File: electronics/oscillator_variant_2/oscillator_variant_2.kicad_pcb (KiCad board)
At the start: 2 copper layers, 42.5 x 46.2 mm, 51 parts, among them J1 module_2x15_left_input, J2 module_2x15_right_input, J3 Coax, Q1 BC817, U1 TL081, U2 LME49720, U3 TL082, U4 TL431

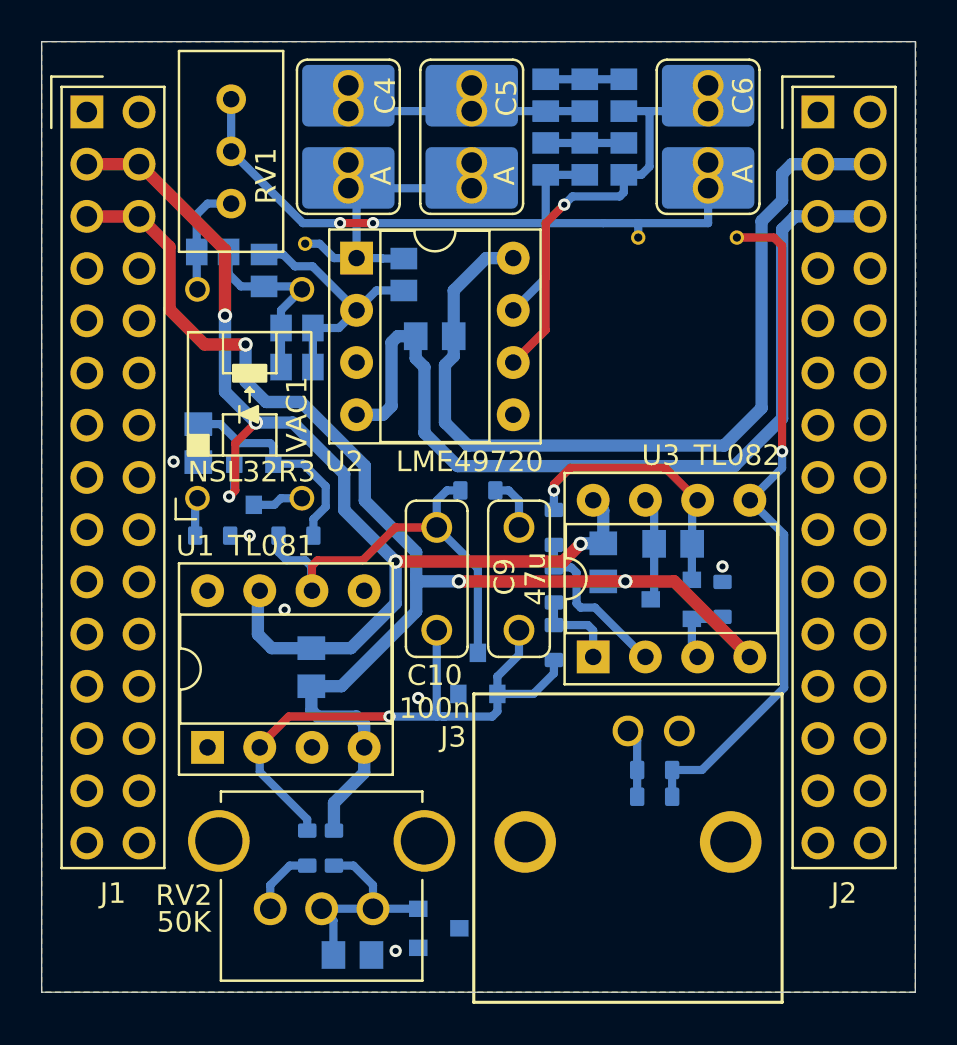
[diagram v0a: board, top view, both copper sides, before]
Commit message: added oscillator variant with dual single opamp
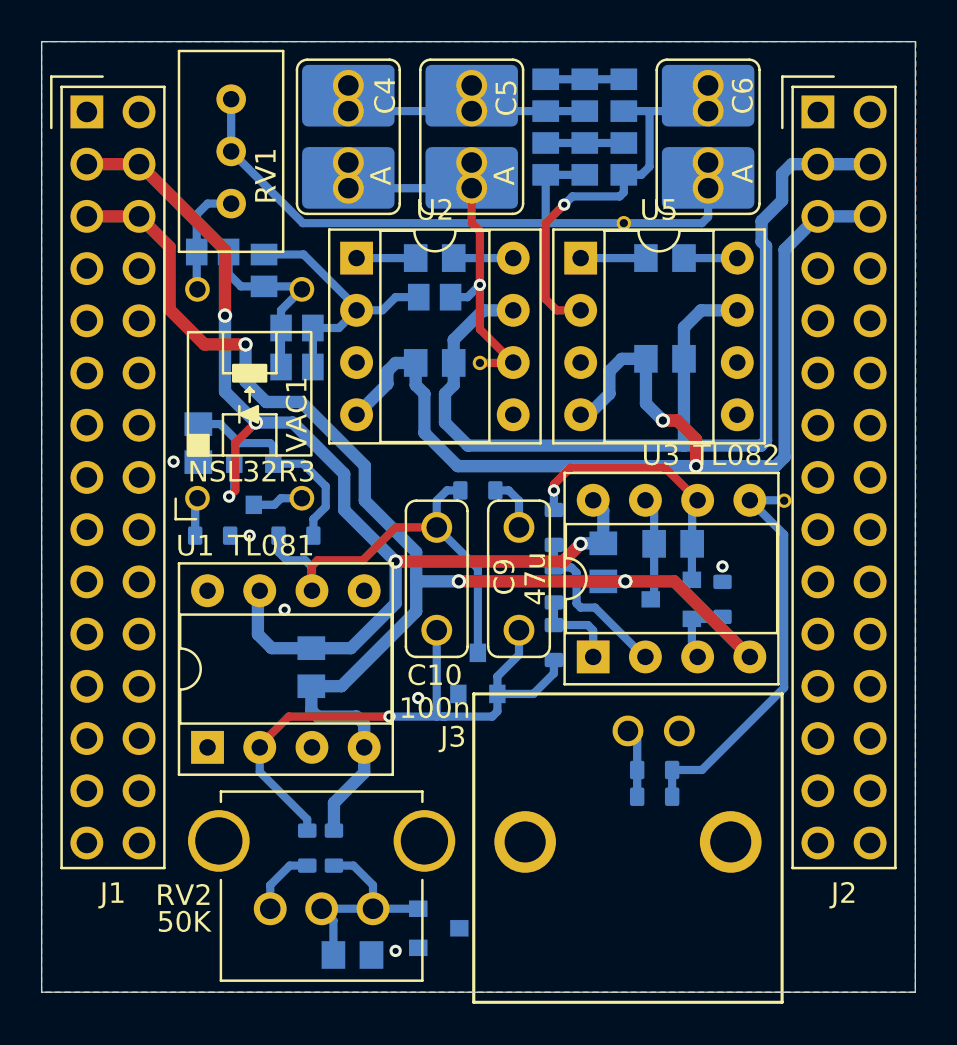
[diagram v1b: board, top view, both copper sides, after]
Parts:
- added C12: 22p, SquantorRcl:C_0805+0603, B.Cu at (161.7, 79.5)
- added C13: 10u, SquantorRcl:C_0805+0603, B.Cu at (172.9, 84.4)
- added C14: 22p, SquantorRcl:C_0805+0603, B.Cu at (172.9, 79.5)
- added U5: NE5534, Package_DIP:DIP-8_W7.62mm_Socket, F.Cu at (168.8, 79.5)
- U2: value LME49720 -> NE5534
- moved TP3 13.0 mm to (178.7, 91.3)
- moved TP1 10.3 mm to (163.9, 84.6)
- moved R12 1.86 mm to (161.7, 81.4), turned to 0 degrees
- moved C2 1.30 mm to (161.7, 84.6)
- moved TP2 0.99 mm to (170.9, 77.8)
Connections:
- U2 pad 1: /OUT_GAIN -> Net-(C12-Pad1)
- U2 pad 5: GND -> unconnected-(U2-Pad5)
- U2 pad 6: Net-(C6-Pad1) -> /OUT_GAIN
- U2 pad 7: /OUT_BRIDGE -> /+15_OSC
- U2 pad 8: /+15_OSC -> Net-(C12-Pad2)
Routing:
- net /OUTPUT: track 33.6 -> 19.9 mm, vias 1 -> 0
- net /-15_OSC: track 43.9 -> 52.7 mm, vias 0 -> 2
- net /+15_OSC: track 43.1 -> 50.5 mm
- net /OUT_BRIDGE: track 38.7 -> 33.0 mm, vias 2 -> 0
- net /OUT_GAIN: track 14.7 -> 18.6 mm, vias 0 -> 1
- net Net-(C14-Pad1): track 0.00 -> 3.17 mm
- net Net-(C12-Pad2): track 0.00 -> 2.90 mm
- net Net-(C12-Pad1): track 0.00 -> 2.88 mm
- net Net-(C14-Pad2): track 0.00 -> 2.59 mm
- net Net-(C6-Pad1): track 20.9 -> 19.1 mm
- net Net-(R11-Pad2): track 12.7 -> 13.4 mm

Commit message: completed place and routing
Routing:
- net /OUT_BRIDGE: track 33.0 -> 42.0 mm
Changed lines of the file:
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@@
   (segment (start 169.5 96.5) (end 171.9 98.9) (width 0.4) (layer "B.Cu") (net 51))
   (segment (start 173.825 84.4) (end 173.825 82.875) (width 0.6) (layer "B.Cu") (net 52))
-  (segment (start 178.6 75.4) (end 178.6 76.7) (width 0.6) (layer "B.Cu") (net 52))
+  (segment (start 177.58 88.62) (end 173.82 88.62) (width 0.6) (layer "B.Cu") (net 52))
   (segment (start 162.625 85.675) (end 162.625 84.6) (width 0.6) (layer "B.Cu") (net 52))
   (segment (start 173.82 88.62) (end 163.32 88.62) (width 0.6) (layer "B.Cu") (net 52))
   (segment (start 182.88 74.93) (end 180.34 74.93) (width 0.6) (layer "B.Cu") (net 52))
-  (segment (start 177.58 88.62) (end 173.82 88.62) (width 0.6) (layer "B.Cu") (net 52))
+  (segment (start 177.82 88.38) (end 177.58 88.62) (width 0.6) (layer "B.Cu") (net 52))
   (segment (start 162.625 84.6) (end 162.625 83.475) (width 0.6) (layer "B.Cu") (net 52))
   (segment (start 163.32 88.62) (end 162.2 87.5) (width 0.6) (layer "B.Cu") (net 52))
-  (segment (start 179.07 74.93) (end 178.6 75.4) (width 0.6) (layer "B.Cu") (net 52))
   (segment (start 173.825 88.615) (end 173.82 88.62) (width 0.6) (layer "B.Cu") (net 52))
+  (segment (start 178.6 77.3) (end 177.82 78.08) (width 0.6) (layer "B.Cu") (net 52))
   (segment (start 162.2 87.5) (end 162.2 86.1) (width 0.6) (layer "B.Cu") (net 52))
   (segment (start 162.2 86.1) (end 162.625 85.675) (width 0.6) (layer "B.Cu") (net 52))
   (segment (start 164.06 82.04) (end 165.52 82.04) (width 0.6) (layer "B.Cu") (net 52))
-  (segment (start 180.34 74.93) (end 179.07 74.93) (width 0.6) (layer "B.Cu") (net 52))
   (segment (start 174.66 82.04) (end 176.42 82.04) (width 0.6) (layer "B.Cu") (net 52))
-  (segment (start 177.82 78.920101) (end 177.82 88.38) (width 0.6) (layer "B.Cu") (net 52))
-  (segment (start 177.82 88.38) (end 177.58 88.62) (width 0.6) (layer "B.Cu") (net 52))
-  (segment (start 177.6 78.700101) (end 177.82 78.920101) (width 0.6) (layer "B.Cu") (net 52))
+  (segment (start 179.07 74.93) (end 178.6 75.4) (width 0.6) (layer "B.Cu") (net 52))
   (segment (start 162.625 83.475) (end 164.06 82.04) (width 0.6) (layer "B.Cu") (net 52))
   (segment (start 173.825 84.4) (end 173.825 88.615) (width 0.6) (layer "B.Cu") (net 52))
   (segment (start 173.825 82.875) (end 174.66 82.04) (width 0.6) (layer "B.Cu") (net 52))
-  (segment (start 177.6 77.7) (end 177.6 78.700101) (width 0.6) (layer "B.Cu") (net 52))
-  (segment (start 178.6 76.7) (end 177.6 77.7) (width 0.6) (layer "B.Cu") (net 52))
+  (segment (start 177.82 78.08) (end 177.82 88.38) (width 0.6) (layer "B.Cu") (net 52))
+  (segment (start 178.6 75.4) (end 178.6 77.3) (width 0.6) (layer "B.Cu") (net 52))
+  (segment (start 180.34 74.93) (end 179.07 74.93) (width 0.6) (layer "B.Cu") (net 52))
   (segment (start 174.419501 88.319501) (end 174.419501 89.619501) (width 0.6) (layer "F.Cu") (net 53))
   (segment (start 173.5 87.4) (end 174.419501 88.319501) (width 0.6) (layer "F.Cu") (net 53))
@@
   (via (at 172.8 87.4) (size 0.7) (drill 0.4) (layers "F.Cu" "B.Cu") (net 53))
   (via (at 174.419501 89.619501) (size 0.7) (drill 0.4) (layers "F.Cu" "B.Cu") (net 53))
-  (segment (start 178.719501 89.180499) (end 178.280499 89.619501) (width 0.6) (layer "B.Cu") (net 53))
+  (segment (start 180.34 77.47) (end 178.899501 78.910499) (width 0.6) (layer "B.Cu") (net 53))
   (segment (start 182.88 77.47) (end 180.34 77.47) (width 0.6) (layer "B.Cu") (net 53))
+  (segment (start 160.775 85.675) (end 160.775 84.6) (width 0.6) (layer "B.Cu") (net 53))
   (segment (start 171.975 86.575) (end 172.8 87.4) (width 0.6) (layer "B.Cu") (net 53))
-  (segment (start 180.34 77.47) (end 178.719501 79.090499) (width 0.6) (layer "B.Cu") (net 53))
+  (segment (start 161.2 88) (end 161.2 86.1) (width 0.6) (layer "B.Cu") (net 53))
   (segment (start 170.8 84.4) (end 170.2 85) (width 0.6) (layer "B.Cu") (net 53))
   (segment (start 159.4 85.62) (end 157.9 87.12) (width 0.6) (layer "B.Cu") (net 53))
-  (segment (start 178.719501 79.090499) (end 178.719501 89.180499) (width 0.6) (layer "B.Cu") (net 53))
   (segment (start 159.4 85) (end 159.4 85.62) (width 0.6) (layer "B.Cu") (net 53))
-  (segment (start 161.2 88) (end 161.2 86.1) (width 0.6) (layer "B.Cu") (net 53))
-  (segment (start 161.2 86.1) (end 160.775 85.675) (width 0.6) (layer "B.Cu") (net 53))
+  (segment (start 178.899501 89.000499) (end 178.280499 89.619501) (width 0.6) (layer "B.Cu") (net 53))
   (segment (start 170.2 86.1) (end 169.18 87.12) (width 0.6) (layer "B.Cu") (net 53))
-  (segment (start 162.819501 89.619501) (end 161.2 88) (width 0.6) (layer "B.Cu") (net 53))
-  (segment (start 160.775 85.675) (end 160.775 84.6) (width 0.6) (layer "B.Cu") (net 53))
+  (segment (start 178.280499 89.619501) (end 162.819501 89.619501) (width 0.6) (layer "B.Cu") (net 53))
   (segment (start 159.8 84.6) (end 159.4 85) (width 0.6) (layer "B.Cu") (net 53))
   (segment (start 171.975 84.4) (end 171.975 86.575) (width 0.6) (layer "B.Cu") (net 53))
+  (segment (start 162.819501 89.619501) (end 161.2 88) (width 0.6) (layer "B.Cu") (net 53))
   (segment (start 171.975 84.4) (end 170.8 84.4) (width 0.6) (layer "B.Cu") (net 53))
   (segment (start 169.18 87.12) (end 168.8 87.12) (width 0.6) (layer "B.Cu") (net 53))
   (segment (start 160.775 84.6) (end 159.8 84.6) (width 0.6) (layer "B.Cu") (net 53))
-  (segment (start 178.280499 89.619501) (end 162.819501 89.619501) (width 0.6) (layer "B.Cu") (net 53))
+  (segment (start 161.2 86.1) (end 160.775 85.675) (width 0.6) (layer "B.Cu") (net 53))
   (segment (start 170.2 85) (end 170.2 86.1) (width 0.6) (layer "B.Cu") (net 53))
+  (segment (start 178.899501 78.910499) (end 178.899501 89.000499) (width 0.6) (layer "B.Cu") (net 53))
   (segment (start 162.625 79.5) (end 165.52 79.5) (width 0.4) (layer "B.Cu") (net 54))
+  (segment (start 176.42 84.58) (end 175 83.16) (width 0.4) (layer "F.Cu") (net 55))
+  (segment (start 175 83.16) (end 175 76.1) (width 0.4) (layer "F.Cu") (net 55))
   (segment (start 167.1 77.8) (end 174.7 77.8) (width 0.4) (layer "B.Cu") (net 55))
   (segment (start 151.8 71.77) (end 151.8 74.31) (width 0.4) (layer "B.Cu") (net 55))

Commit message: silk placement completed
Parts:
- added N3: Freq, SquantorLabels:Label_Note_medium, F.Cu at (166.2, 74.9)
- moved TP3 1.22 mm to (178.5, 90.1)
- moved TP2 0.40 mm to (170.5, 77.8)
- moved R20 0.30 mm to (163.8, 91.1)
- moved R17 0.20 mm to (156.8, 108.4)
- moved R19 0.20 mm to (155.5, 108.4)
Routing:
- net /-15_OSC: track 52.7 -> 50.8 mm

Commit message: review completed
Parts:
- moved TP1 2.12 mm to (163.6, 86.7)
- moved TP2 1.03 mm to (171.4, 77.3)
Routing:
- net /OUT_GAIN: track 18.6 -> 19.9 mm
- net /OUTPUT: track 20.2 -> 21.0 mm
- net /OUT_BRIDGE: track 42.0 -> 42.5 mm
- net GND: vias 6 -> 7

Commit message: small changes in output pin
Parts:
- moved TP3 3.53 mm to (177.0, 93.3)
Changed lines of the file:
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@@
   )
   (footprint "SquantorTestPoints:TestPoint_hole_H04R07" (layer "B.Cu")
-    (at 178.5 90.1 180)
+    (at 177 93.3 180)
     (descr "Test point with 0.4mm hole and 0.7mm annular ring")
     (tags "Test point hole 0.4mm")
@@
       (effects (font (size 1 1) (thickness 0.15)) (justify mirror))
     )
-    (fp_text value "output" (at 0.4 3.6 270) (layer "B.SilkS")
+    (fp_text value "output" (at -1.3 2.7 270) (layer "B.SilkS")
       (effects (font (size 1 1) (thickness 0.15)) (justify mirror))
     )
@@
   (segment (start 167.1 72.35) (end 169 72.35) (width 0.4) (layer "B.Cu") (net 30))
   (segment (start 167.1 72.35) (end 163.5 72.35) (width 0.4) (layer "B.Cu") (net 30))
-  (segment (start 177.32 91.28) (end 178.5 90.1) (width 0.4) (layer "B.Cu") (net 31))
+  (segment (start 177.03 91.28) (end 177.03 93.27) (width 0.4) (layer "B.Cu") (net 31))
+  (segment (start 177.03 93.27) (end 177 93.3) (width 0.4) (layer "B.Cu") (net 31))
   (segment (start 173.9 105.7) (end 178.7 100.9) (width 0.4) (layer "B.Cu") (net 31))
   (segment (start 178.7 100.9) (end 178.7 92.95) (width 0.4) (layer "B.Cu") (net 31))
-  (segment (start 177.03 91.28) (end 177.32 91.28) (width 0.4) (layer "B.Cu") (net 31))
   (segment (start 173.25 105.7) (end 173.25 104.4) (width 0.4) (layer "B.Cu") (net 31))
   (segment (start 173.25 105.7) (end 173.9 105.7) (width 0.4) (layer "B.Cu") (net 31))

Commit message: fixed aisler warnings/errors
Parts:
- C4, C5, C6: footprint SquantorRcl:C-025_050-050X100-0805-3516-film -> SquantorRcl:C-050-050X100-0805-3516-film
- N1: value 20220501 -> 20220530
